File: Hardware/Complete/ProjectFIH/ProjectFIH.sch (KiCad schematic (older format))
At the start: 62 parts, among them J1 Conn_01x02_Male, J2 Heater, J3 Payload, Q1 2N7002, Q2 2N7002, Q3 IRLZ44N, U1 74HC04, U2 LM158, U3 74HC4017, U4 74HC02, U5 74HC08, U6 LM22675-5.0, U7 LM2576S-ADJ

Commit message: Schematic seems to be completed
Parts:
- removed C1: 100uF, symbol Device:CP
- removed D2: 1N4148, Diode_THT:D_DO-35_SOD27_P7.62mm_Horizontal, symbol Diode:1N4148
- added C?: 1uF, symbol Device:C
- added C? (x2): 16pF, symbol Device:C
- added C?: 100nF, symbol Device:C
- added C? (x2): 2.2uF, symbol Device:C
- added C?: 1000uFx50V, symbol Device:CP
- added D? (x2): 1N4148, Diode_THT:D_DO-35_SOD27_P7.62mm_Horizontal, symbol Diode:1N4148
- added J?: AVR-ISP-10, symbol Connector:AVR-ISP-10
- added J?: UART, symbol Connector:Conn_01x03_Male
- added J?: Power, symbol Connector:Screw_Terminal_01x02
- added R12: 470, symbol Device:R
- added R?: 10k, symbol Device:R
- added U? (x2): 74HC04, symbol 74xx:74HC04
- added U? (x2): 74HC02, symbol 74xx:74HC02
- added U? (x2): 74HC08, symbol Fossa_library:74HC08
- added U?: ATmega8A-AU, Package_QFP:TQFP-32_7x7mm_P0.8mm, symbol MCU_Microchip_ATmega:ATmega8A-AU
- added Y?: 8MHz, symbol Device:Crystal
- gave numbers to parts that had none: 1
- renumbered D3 to D2, D4 to D3, D5 to D4, R14 to R13, R12 to R14, R13 to R15, R15 to R16, R16 to R17, R17 to R18, R18 to R19, R19 to R20, R20 to R21, R7 to R5, R5 to R6, R6 to R7
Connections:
- net +24V: now also C?.1, C?.1, J?.1 (Pin_1)
- net +5V: now also U1.11, C?.1, R?.1, U?.10, U?.11, U?.12, U?.12, U?.13, U?.13, U?.18 (AVCC), U?.4 (VCC), U?.6 (VCC), U?.8, U?.9, U?.9
- net GND: now also C?.2, C?.2, C?.2, C?.2, C?.2, C?.2, C?.2, J?.10 (GND), J?.2 (Pin_2), J?.3 (Pin_3), J?.4 (GND), J?.6 (GND), J?.8 (GND), U?.21 (AGND), U?.3 (GND), U?.5 (GND)
- net IRQ: now also D?.2 (A)
- net IRQResp: now also U?.1 (PD3)
- net MCUReset: now also C?.1, D?.2 (A), J?.5 (~RST), R?.2, U?.29 (PC6/~RESET)
- net MCU_PL_ON: now also U?.9 (PD5)
- net PL_ON: now also U1.8; no longer U1.10
- net Temperature: now reaches R6.1, R8.2, U2.1
- net Temperature: now also U?.23 (PC0)
- net at U3.11 (Q9), U4.2: now also U?.5; no longer U1.9
- net at U5.6: now also U1.9; no longer U1.11
- new net: D?.1 (K), R12.1
- new net: R12.2, U?.6
- new net: J?.1 (MOSI), U?.15 (PB3)
- new net: J?.9 (MISO), U?.16 (PB4)
- new net: J?.7 (SCK), U?.17 (PB5)
- new net: C?.1, U?.20 (AREF)
- new net: J?.1 (Pin_1), U?.30 (PD0)
- new net: J?.2 (Pin_2), U?.31 (PD1)
- new net: D?.1 (K), U?.32 (PD2)
- new net: C?.1, U?.7 (PB6/XTAL1), Y?.2
- new net: C?.1, U?.8 (PB7/XTAL2), Y?.1
- new net MCUHeatOff: U?.2 (PD4)
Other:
- note added: "+"
- note added: "24V IN"
- note added: "GND"
- note added: "Hardware watchdog"
- note added: "MCU"
- note added: "Overheat protection / backup thermostat"
- note added: "Programming"
- note added: "RX"
- note added: "Shifting amplifier"
- note added: "TX"
- note added: "Unused"
- moved on the sheet: U1D, U1E, U2C

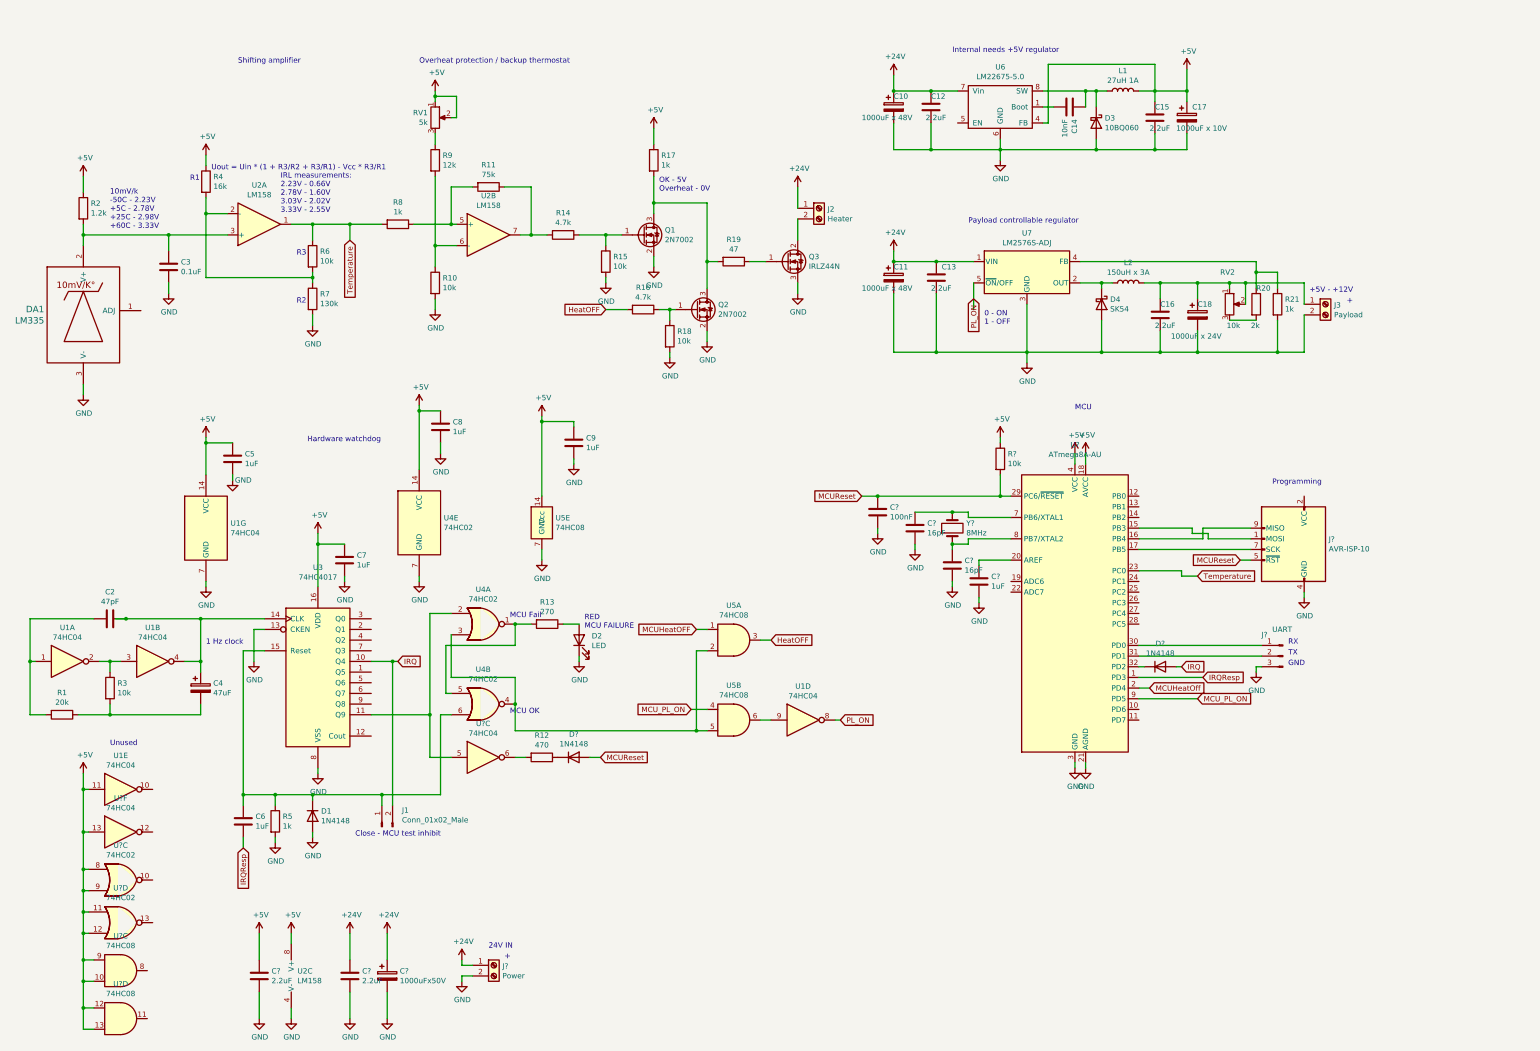
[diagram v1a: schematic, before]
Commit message: Added LEDs
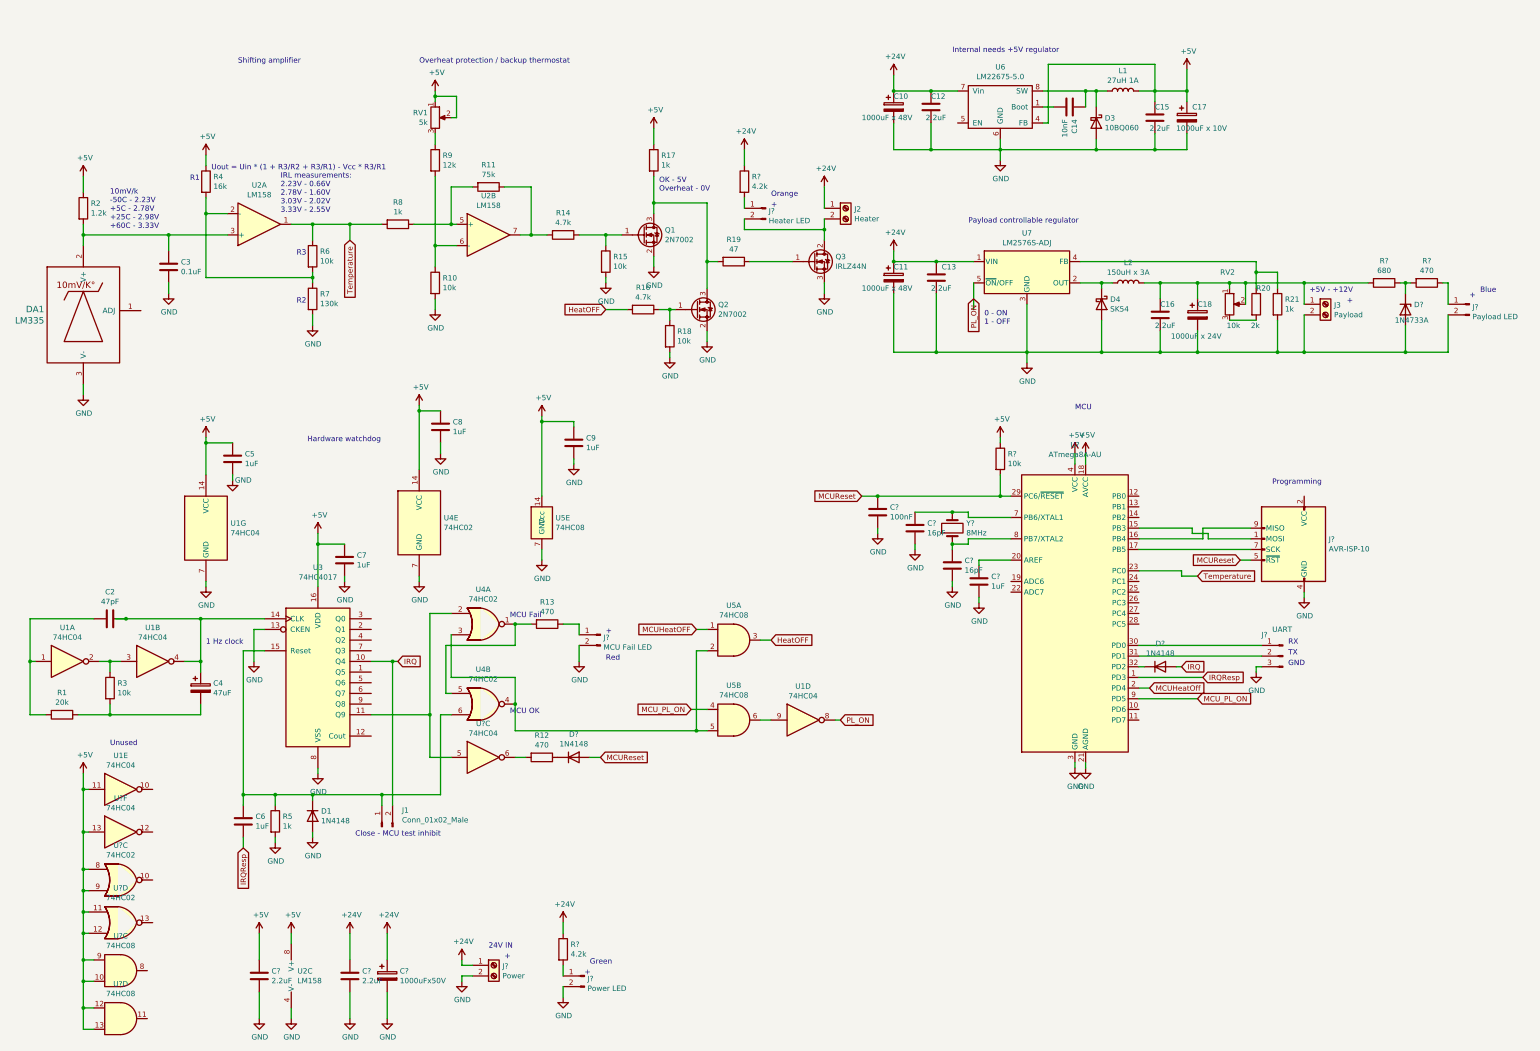
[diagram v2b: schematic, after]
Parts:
- removed D2: LED, symbol Device:LED
- added D?: 1N4733A, Diode_THT:D_DO-41_SOD81_P10.16mm_Horizontal, symbol Diode:1N47xxA
- added J?: MCU Fail LED, symbol Connector:Conn_01x02_Male
- added J?: Power LED, symbol Connector:Conn_01x02_Male
- added J?: Heater LED, symbol Connector:Conn_01x02_Male
- added J?: Payload LED, symbol Connector:Conn_01x02_Male
- added R? (x2): 4.2k, symbol Device:R
- added R?: 680, symbol Device:R
- added R?: 470, symbol Device:R
- R13: value 270 -> 470
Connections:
- net +24V: now also R?.1, R?.1
- net GND: now also D?.2 (A), J?.2 (Pin_2), J?.2 (Pin_2), J?.2 (Pin_2)
- net at J2.2 (Pin_2), Q3.2 (D): now also J?.2 (Pin_2)
- net at C16.1, C18.1, J3.1 (Pin_1)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: now also R?.2
- net at R13.1: now also J?.1 (Pin_1)
- new net: J?.1 (Pin_1), R?.2 (x2)
- new net: D?.1 (K), R?.1, R?.2
- new net: J?.1 (Pin_1), R?.1
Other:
- note added: "Blue"
- note added: "Green"
- note added: "Orange"
- note added: "Red"
- note removed: "RED\nMCU FAILURE"
- moved on the sheet: J2, Q3

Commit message: Assigned some cases
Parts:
- added C21: 1uF, Capacitor_SMD:C_0805_2012Metric_Pad1.15x1.40mm_HandSolder, symbol Device:C
- C1: renamed from C2; footprint (none) -> Capacitor_SMD:C_0805_2012Metric_Pad1.15x1.40mm_HandSolder
- C10: renamed from C8; footprint (none) -> Capacitor_SMD:C_0805_2012Metric_Pad1.15x1.40mm_HandSolder
- C11: renamed from C9; footprint (none) -> Capacitor_SMD:C_0805_2012Metric_Pad1.15x1.40mm_HandSolder
- C12, C15, C18, C19, C6, C8: renamed from C?; footprint (none) -> Capacitor_SMD:C_0805_2012Metric_Pad1.15x1.40mm_HandSolder
- C13: renamed from C10; footprint (none) -> Capacitor_THT:CP_Radial_D12.5mm_P7.50mm
- C14: renamed from C11; footprint (none) -> Capacitor_THT:CP_Radial_D12.5mm_P7.50mm
- C16: renamed from C12; footprint (none) -> Capacitor_SMD:C_0805_2012Metric_Pad1.15x1.40mm_HandSolder
- C17: renamed from C13; footprint (none) -> Capacitor_SMD:C_0805_2012Metric_Pad1.15x1.40mm_HandSolder
- C2: renamed from C3; footprint (none) -> Capacitor_SMD:C_0805_2012Metric_Pad1.15x1.40mm_HandSolder
- C20: renamed from C14; footprint (none) -> Capacitor_SMD:C_0805_2012Metric_Pad1.15x1.40mm_HandSolder
- C22: renamed from C15; footprint (none) -> Capacitor_SMD:C_0805_2012Metric_Pad1.15x1.40mm_HandSolder
- C23: renamed from C16; footprint (none) -> Capacitor_SMD:C_0805_2012Metric_Pad1.15x1.40mm_HandSolder
- C24: renamed from C17; footprint (none) -> Capacitor_THT:CP_Radial_D10.0mm_P5.00mm
- C25: renamed from C18; footprint (none) -> Capacitor_THT:CP_Radial_D10.0mm_P5.00mm
- C3: renamed from C4; footprint (none) -> Capacitor_SMD:CP_Elec_4x5.7
- C4: renamed from C5; footprint (none) -> Capacitor_SMD:C_0805_2012Metric_Pad1.15x1.40mm_HandSolder
- C5: renamed from C6; footprint (none) -> Capacitor_SMD:C_0805_2012Metric_Pad1.15x1.40mm_HandSolder
- C7: footprint (none) -> Capacitor_SMD:C_0805_2012Metric_Pad1.15x1.40mm_HandSolder
- C9: renamed from C?; footprint (none) -> Capacitor_THT:CP_Radial_D12.5mm_P7.50mm
- D1: footprint Diode_THT:D_DO-35_SOD27_P7.62mm_Horizontal -> Diode_SMD:D_1210_3225Metric
- D2, D5: renamed from D?; footprint Diode_THT:D_DO-35_SOD27_P7.62mm_Horizontal -> Diode_SMD:D_1210_3225Metric
- D3: footprint (none) -> Diode_SMD:D_SMB
- D4: footprint (none) -> Diode_SMD:D_SMC
- D6: renamed from D?; footprint Diode_THT:D_DO-41_SOD81_P10.16mm_Horizontal -> Diode_SMD:D_1210_3225Metric
- DA1: footprint (none) -> Package_TO_SOT_THT:TO-92
- J1: footprint (none) -> Connector_PinHeader_2.54mm:PinHeader_1x02_P2.54mm_Vertical
- J10, J3, J4, J5: renamed from J?; footprint (none) -> Connector_PinHeader_2.54mm:PinHeader_1x02_P2.54mm_Vertical
- J2: renamed from J?; footprint (none) -> TerminalBlock:TerminalBlock_Altech_AK300-2_P5.00mm
- J6: renamed from J2; footprint (none) -> TerminalBlock:TerminalBlock_Altech_AK300-2_P5.00mm
- J7: renamed from J?; footprint (none) -> Connector_PinHeader_2.54mm:PinHeader_1x03_P2.54mm_Vertical
- J8: renamed from J?; footprint (none) -> Connector_IDC:IDC-Header_2x05_P2.54mm_Vertical
- J9: renamed from J3; footprint (none) -> TerminalBlock:TerminalBlock_Altech_AK300-2_P5.00mm
- gave numbers to parts that had none: 10
- renumbered R15 to R16, R16 to R17, R17 to R18, R18 to R19, R19 to R20, R20 to R23, R21 to R24, U5 to U2, U4 to U3, U2 to U4, U3 to U5
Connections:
- net +5V: now also C21.1
- net GND: now also C21.2

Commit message: Cases assigned
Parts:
- L1: footprint (none) -> Inductor_THT:L_Radial_D10.0mm_P5.00mm_Fastron_07M
- L2: footprint (none) -> Inductor_THT:L_Radial_D16.8mm_P11.43mm_Vishay_IHB-1
- R1, R10, R11, R12, R13, R14, R15, R16, R17, R18, R19, R2, R20, R21, R22, R23, R24, R25, R26, R3, R4, R5, R6, R7, R8, R9: footprint (none) -> Resistor_SMD:R_0805_2012Metric_Pad1.15x1.40mm_HandSolder
- RV1, RV2: footprint (none) -> Potentiometer_THT:Potentiometer_Bourns_3296W_Vertical
- U1, U2, U3: footprint (none) -> Package_SO:SOIC-14_3.9x8.7mm_P1.27mm
- U4: footprint (none) -> Package_SO:SOIJ-8_5.3x5.3mm_P1.27mm
- U5: footprint (none) -> Package_SO:SOIC-16_4.55x10.3mm_P1.27mm
- U6: footprint (none) -> Package_SO:SOIC-8-1EP_3.9x4.9mm_P1.27mm_EP2.29x3mm
- Y1: footprint (none) -> Crystal:Crystal_HC49-4H_Vertical

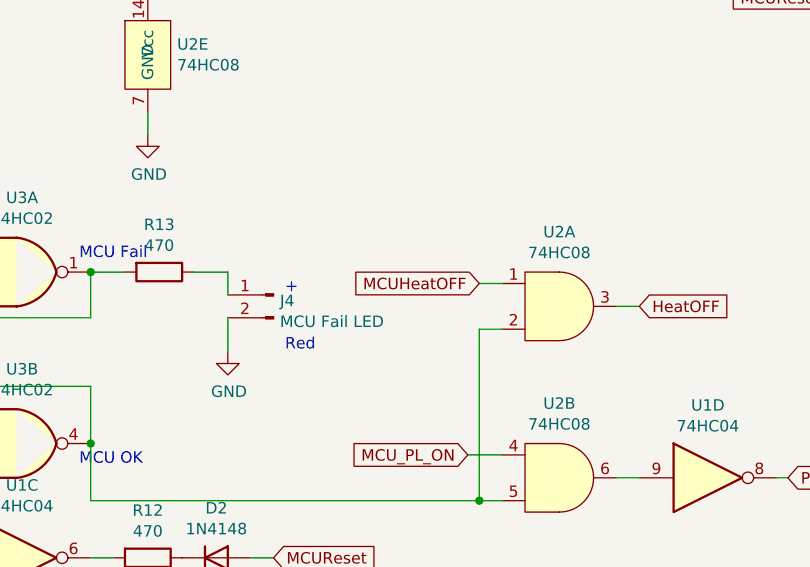
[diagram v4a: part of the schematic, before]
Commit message: Fixed label and generated netlist
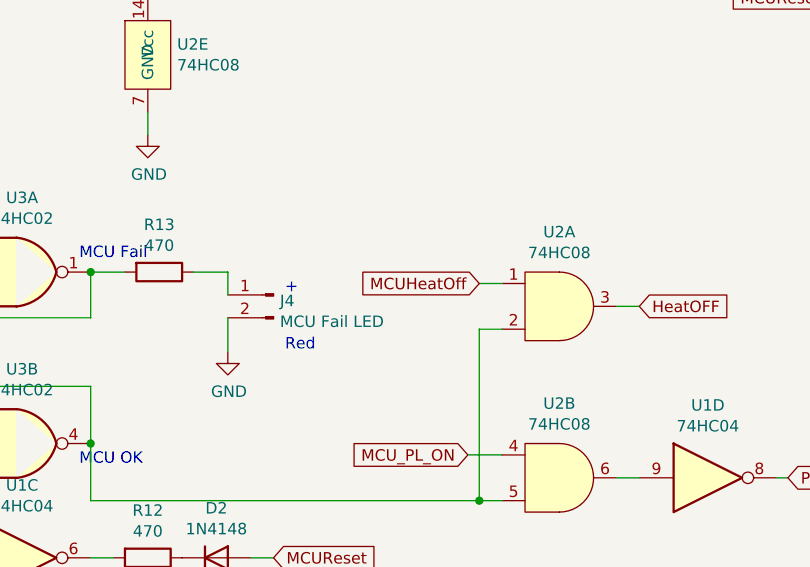
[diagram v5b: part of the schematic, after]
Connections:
- net MCUHeatOFF is gone; now on net MCUHeatOff: U2.1
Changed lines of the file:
@@
 Connection ~ 5300 7000
 Text GLabel 7000 6300 0    50   Input ~ 0
-MCUHeatOFF
+MCUHeatOff
 Wire Wire Line
 	7100 6300 7000 6300

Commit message: Partially routed PCB
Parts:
- R16, R19: value 10k -> 47k
- U6: footprint Package_SO:SOIC-8-1EP_3.9x4.9mm_P1.27mm_EP2.29x3mm -> Package_SO:SOIC-8_3.9x4.9mm_P1.27mm
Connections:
- net +24V: now also J6.2 (Pin_2); no longer J6.1 (Pin_1)
- net at J5.2 (Pin_2), Q3.2 (D): now also J6.1 (Pin_1); no longer J6.2 (Pin_2)
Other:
- moved on the sheet: J6
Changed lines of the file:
@@
 L Connector:Screw_Terminal_01x02 J6
 U 1 1 5F039ABC
-P 8400 2350
-F 0 "J6" H 8480 2342 50  0000 L CNN
-F 1 "Heater" H 8480 2251 50  0000 L CNN
-F 2 "TerminalBlock:TerminalBlock_Altech_AK300-2_P5.00mm" H 8400 2350 50  0001 C CNN
-F 3 "~" H 8400 2350 50  0001 C CNN
-	1    8400 2350
-	1    0    0    -1
-$EndComp
-Wire Wire Line
-	8200 2450 8200 2550
+P 8400 2400
+F 0 "J6" H 8480 2392 50  0000 L CNN
+F 1 "Heater" H 8480 2301 50  0000 L CNN
+F 2 "TerminalBlock:TerminalBlock_Altech_AK300-2_P5.00mm" H 8400 2400 50  0001 C CNN
+F 3 "~" H 8400 2400 50  0001 C CNN
+	1    8400 2400
+	1    0    0    1
+$EndComp
 $Comp
 L power:+24V #PWR043
@@
 	1    0    0    -1
 $EndComp
-Wire Wire Line
-	8200 2150 8200 2350
 $Comp
 L Device:CP C13
@@
 $EndComp
 $Comp
-L Device:C C22
-U 1 1 5F0A7836
-P 11300 1500
-F 0 "C22" H 11300 1600 50  0000 L CNN
-F 1 "2.2uF" H 11250 1400 50  0000 L CNN
-F 2 "Capacitor_SMD:C_0805_2012Metric_Pad1.15x1.40mm_HandSolder" H 11338 1350 50  0001 C CNN
-F 3 "~" H 11300 1500 50  0001 C CNN
-	1    11300 1500
-	1    0    0    -1
-$EndComp
-$Comp
 L Device:CP C24
 U 1 1 5F0A7FA4
@@
 F 0 "U6" H 9850 1375 50  0000 C CNN
 F 1 "LM22675-5.0" H 9850 1284 50  0000 C CNN
-F 2 "Package_SO:SOIC-8-1EP_3.9x4.9mm_P1.27mm_EP2.29x3mm" H 9000 1600 50  0001 C CNN
+F 2 "Package_SO:SOIC-8_3.9x4.9mm_P1.27mm" H 9000 1600 50  0001 C CNN
 F 3 "" H 9000 1600 50  0001 C CNN
 	1    9850 1200
@@
 P 6750 3550
 F 0 "R19" H 6820 3596 50  0000 L CNN
-F 1 "10k" H 6820 3505 50  0000 L CNN
+F 1 "47k" H 6820 3505 50  0000 L CNN
 F 2 "Resistor_SMD:R_0805_2012Metric_Pad1.15x1.40mm_HandSolder" V 6680 3550 50  0001 C CNN
 F 3 "~" H 6750 3550 50  0001 C CNN
@@
 P 6150 2850
 F 0 "R16" H 6220 2896 50  0000 L CNN
-F 1 "10k" H 6220 2805 50  0000 L CNN
+F 1 "47k" H 6220 2805 50  0000 L CNN
 F 2 "Resistor_SMD:R_0805_2012Metric_Pad1.15x1.40mm_HandSolder" V 6080 2850 50  0001 C CNN
 F 3 "~" H 6150 2850 50  0001 C CNN
@@
 Wire Wire Line
 	7450 2550 8200 2550
-Connection ~ 8200 2550
 Wire Wire Line
 	8200 2550 8200 2650
@@
 Wire Wire Line
 	10850 4600 10850 4550
+$Comp
+L Device:C C22
+U 1 1 5F0A7836
+P 11300 1500
+F 0 "C22" H 11300 1600 50  0000 L CNN
+F 1 "2.2uF" H 11250 1400 50  0000 L CNN
+F 2 "Capacitor_SMD:C_0805_2012Metric_Pad1.15x1.40mm_HandSolder" H 11338 1350 50  0001 C CNN
+F 3 "~" H 11300 1500 50  0001 C CNN
+	1    11300 1500
+	1    0    0    -1
+$EndComp
+Wire Wire Line
+	8200 2300 8200 2150
+Wire Wire Line
+	8200 2400 8200 2550
+Connection ~ 8200 2550
 $EndSCHEMATC

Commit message: More tracing
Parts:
- Q3: footprint Package_TO_SOT_THT:TO-220-3_Vertical -> Package_TO_SOT_THT:TO-220-3_Horizontal_TabDown
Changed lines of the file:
@@
 F 0 "Q3" H 8304 2896 50  0000 L CNN
 F 1 "IRLZ44N" H 8304 2805 50  0000 L CNN
-F 2 "Package_TO_SOT_THT:TO-220-3_Vertical" H 8350 2775 50  0001 L CIN
+F 2 "Package_TO_SOT_THT:TO-220-3_Horizontal_TabDown" H 8350 2775 50  0001 L CIN
 F 3 "http://www.irf.com/product-info/datasheets/data/irlz44n.pdf" H 8100 2850 50  0001 L CNN
 	1    8100 2850

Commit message: More tracing
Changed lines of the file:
@@
 Wire Wire Line
 	8350 7150 8300 7150
-Connection ~ 1650 6200
-Wire Wire Line
-	1650 6200 1550 6200
 Wire Wire Line
 	2750 6500 2950 6500
